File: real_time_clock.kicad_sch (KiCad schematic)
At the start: 4 parts, among them U7 PCF85063A, Y2 Crystal

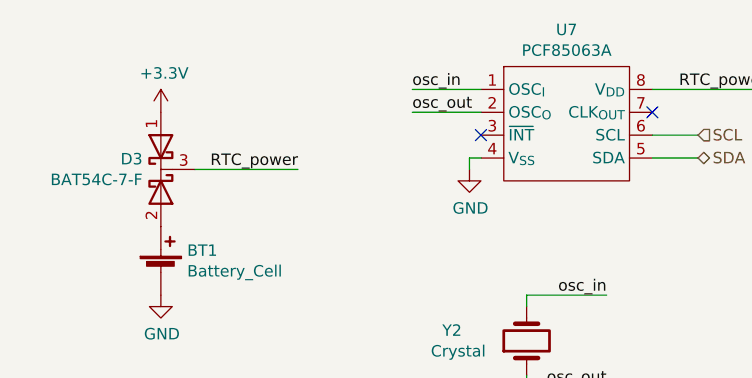
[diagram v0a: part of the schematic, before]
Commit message: more layout: power supply and gpio
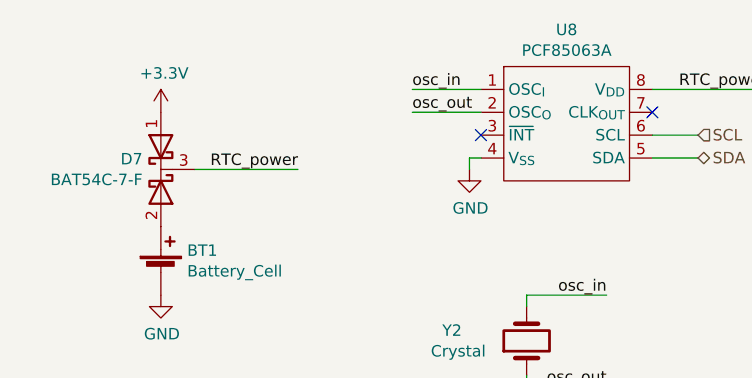
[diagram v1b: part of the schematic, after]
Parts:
- U8: renamed from U7; footprint (none) -> Package_SO:SOIC-8_3.9x4.9mm_P1.27mm
- renumbered D3 to D7
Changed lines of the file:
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@@
   (symbol (lib_id "power:+3.3V") (at 62.23 104.14 0) (unit 1)
     (in_bom yes) (on_board yes)
-    (property "Reference" "#PWR0155" (id 0) (at 62.23 107.95 0)
+    (property "Reference" "#PWR0164" (id 0) (at 62.23 107.95 0)
       (effects (font (size 1.27 1.27)) hide)
     )
@@
   (symbol (lib_id "power:GND") (at 62.23 124.46 0) (unit 1)
     (in_bom yes) (on_board yes)
-    (property "Reference" "#PWR0154" (id 0) (at 62.23 130.81 0)
+    (property "Reference" "#PWR0163" (id 0) (at 62.23 130.81 0)
       (effects (font (size 1.27 1.27)) hide)
     )
@@
   (symbol (lib_id "power:GND") (at 96.52 110.49 0) (unit 1)
     (in_bom yes) (on_board yes)
-    (property "Reference" "#PWR0156" (id 0) (at 96.52 116.84 0)
+    (property "Reference" "#PWR0165" (id 0) (at 96.52 116.84 0)
       (effects (font (size 1.27 1.27)) hide)
     )
@@
   (symbol (lib_id "symbols:BAT54C-7-F") (at 62.23 110.49 0) (unit 1)
     (in_bom yes) (on_board yes)
-    (property "Reference" "D3" (id 0) (at 60.198 109.3406 0)
+    (property "Reference" "D7" (id 0) (at 60.198 109.3406 0)
       (effects (font (size 1.27 1.27)) (justify right))
     )
@@
   (symbol (lib_id "symbols:PCF85063A") (at 107.95 105.41 0) (unit 1)
     (in_bom yes) (on_board yes)
-    (property "Reference" "U7" (id 0) (at 107.315 94.9765 0))
+    (property "Reference" "U8" (id 0) (at 107.315 94.9765 0))
     (property "Value" "PCF85063A" (id 1) (at 107.315 97.2752 0))
-    (property "Footprint" "" (id 2) (at 101.6 102.87 0)
+    (property "Footprint" "Package_SO:SOIC-8_3.9x4.9mm_P1.27mm" (id 2) (at 101.6 102.87 0)
       (effects (font (size 1.27 1.27)) hide)
     )

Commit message: Finished trace routing
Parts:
- removed Y2: Crystal, symbol Device:Crystal
- added JP6, JP7: SolderJumper_3_Open, Jumper:SolderJumper-3_P1.3mm_Open_RoundedPad1.0x1.5mm_NumberLabels, symbol Jumper:SolderJumper_3_Open
- added U10: TCN75, Package_SO:SOIC-8_3.9x4.9mm_P1.27mm, symbol symbols:TCN75
- added Y3: Crystal-CM7V-T1A-32.768kHz, footprints:Crystal-CM7V, symbol symbols:Crystal-CM7V-T1A-32.768kHz
- renumbered D7 to D9, U8 to U9
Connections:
- net GND: now also JP6.3 (B), JP7.3 (B), U10.4 (GND)
- net osc_in: now also Y3.1
- net osc_out: now also Y3.2
- net SCL renamed SCL_{3.3V}
- net SDA renamed SDA_{3.3V}
- new net: JP7.2 (C), U10.5 (A2)
- new net: JP6.2 (C), U10.6 (A1)
- new net +5V: JP6.1 (A), JP7.1 (A), U10.7 (A0), U10.8 (VDD)
- new net SCL_{5V}: U10.2 (SCL)
- new net SDA_{5V}: U10.1 (SDA)
- no-connect marks 2 -> 3
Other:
- note added: "Address Select Jumpers"
- moved on the sheet: BT1, D9, U9

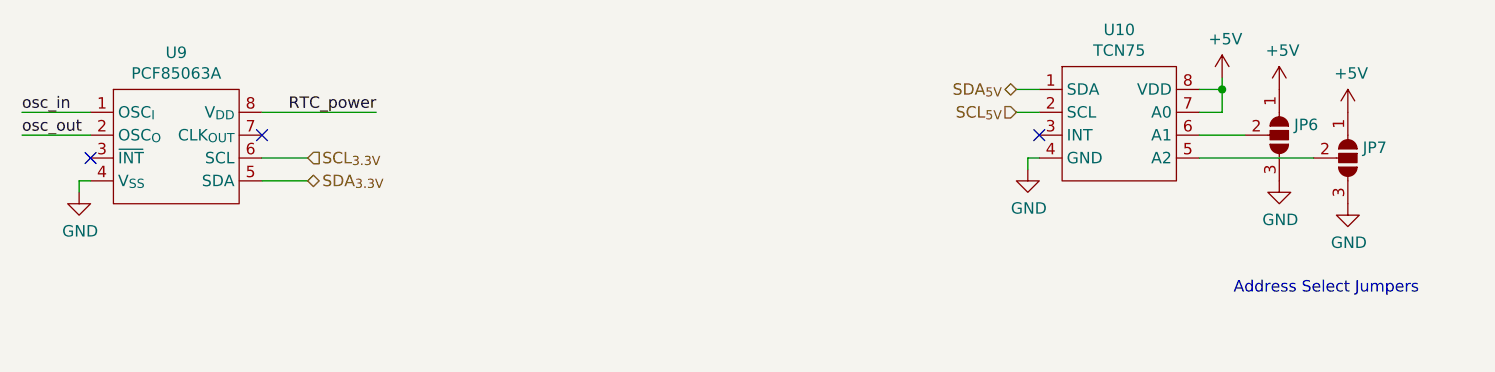
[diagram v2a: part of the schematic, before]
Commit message: Cleaning up
Reassigned reference designators to better match their position on the board.
Moved USB hub IC and related circuits to their own sheet in the schematic.
Tweaked reference designator positions on board to improve visibility.
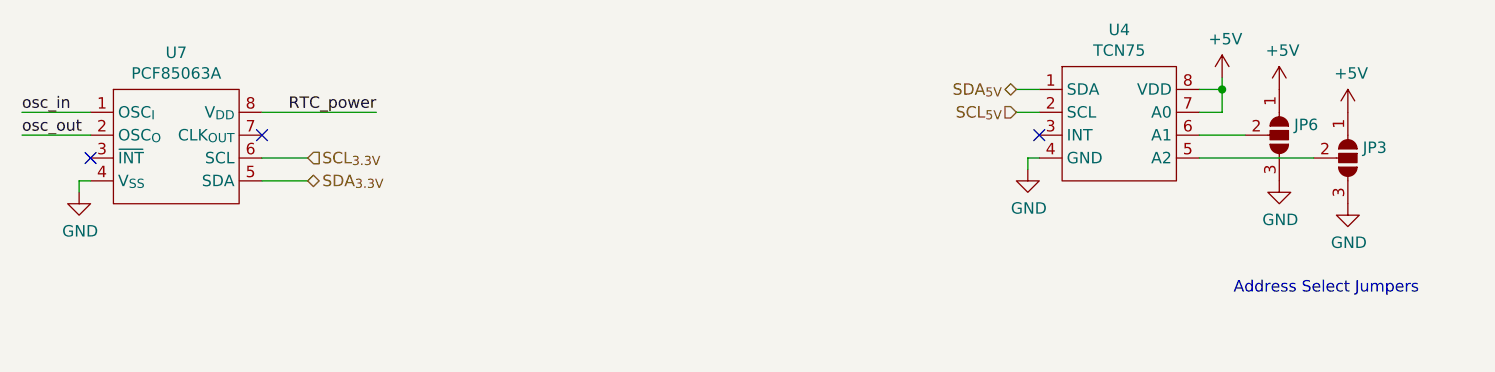
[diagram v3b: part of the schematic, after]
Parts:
- renumbered JP7 to JP3, U10 to U4, U9 to U7
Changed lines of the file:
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@@
   (title_block
     (title "Dennis")
-    (date "2021-02-26")
-    (rev "0.1.2")
+    (date "2021-03-30")
+    (rev "0.1.3")
     (company "eCafe Racer")
   )
   (junction (at 189.23 83.82) (diameter 0.9144) (color 0 0 0 0))
+  (no_connect (at 82.55 88.9))
   (no_connect (at 168.91 88.9))
-  (no_connect (at 82.55 88.9))
   (no_connect (at 63.5 91.44))
   (wire (pts (xy 55.88 86.36) (xy 63.5 86.36))
@@
   (symbol (lib_id "Jumper:SolderJumper_3_Open") (at 203.2 91.44 270) (unit 1)
     (in_bom yes) (on_board yes)
-    (property "Reference" "JP7" (id 0) (at 204.8511 90.2906 90)
+    (property "Reference" "JP3" (id 0) (at 204.8511 90.2906 90)
       (effects (font (size 1.27 1.27)) (justify left))
     )
@@
   (symbol (lib_id "symbols:TCN75") (at 177.8 87.63 0) (unit 1)
     (in_bom yes) (on_board yes)
-    (property "Reference" "U10" (id 0) (at 177.8 77.1965 0))
+    (property "Reference" "U4" (id 0) (at 177.8 77.1965 0))
     (property "Value" "TCN75" (id 1) (at 177.8 79.4952 0))
     (property "Footprint" "Package_SO:SOIC-8_3.9x4.9mm_P1.27mm" (id 2) (at 168.91 83.82 0)
@@
   (symbol (lib_id "symbols:PCF85063A") (at 73.66 90.17 0) (unit 1)
     (in_bom yes) (on_board yes)
-    (property "Reference" "U9" (id 0) (at 73.025 79.7365 0))
+    (property "Reference" "U7" (id 0) (at 73.025 79.7365 0))
     (property "Value" "PCF85063A" (id 1) (at 73.025 82.0352 0))
     (property "Footprint" "Package_SO:SOIC-8_3.9x4.9mm_P1.27mm" (id 2) (at 67.31 87.63 0)

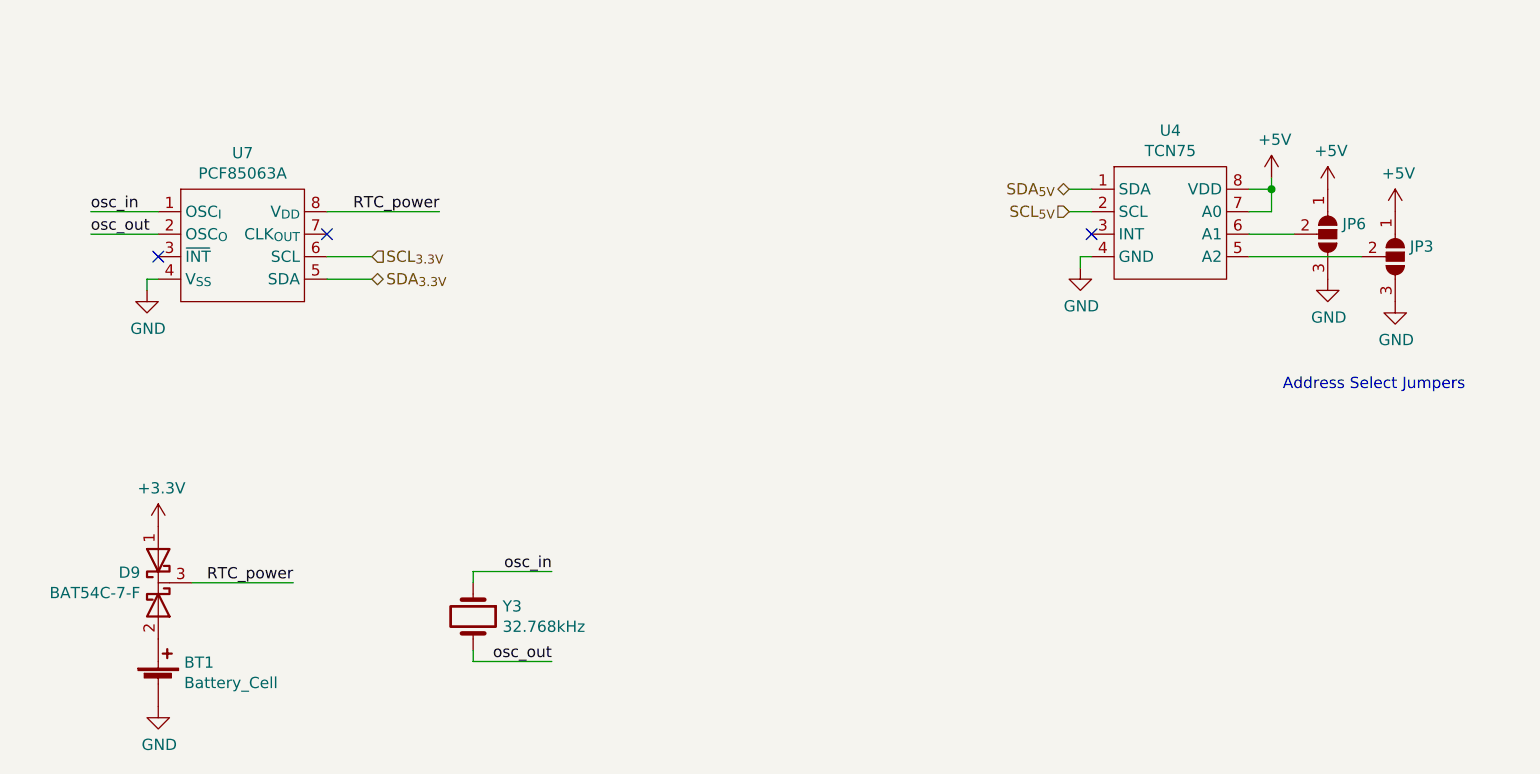
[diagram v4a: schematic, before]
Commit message: components group and placed in roughly the right position
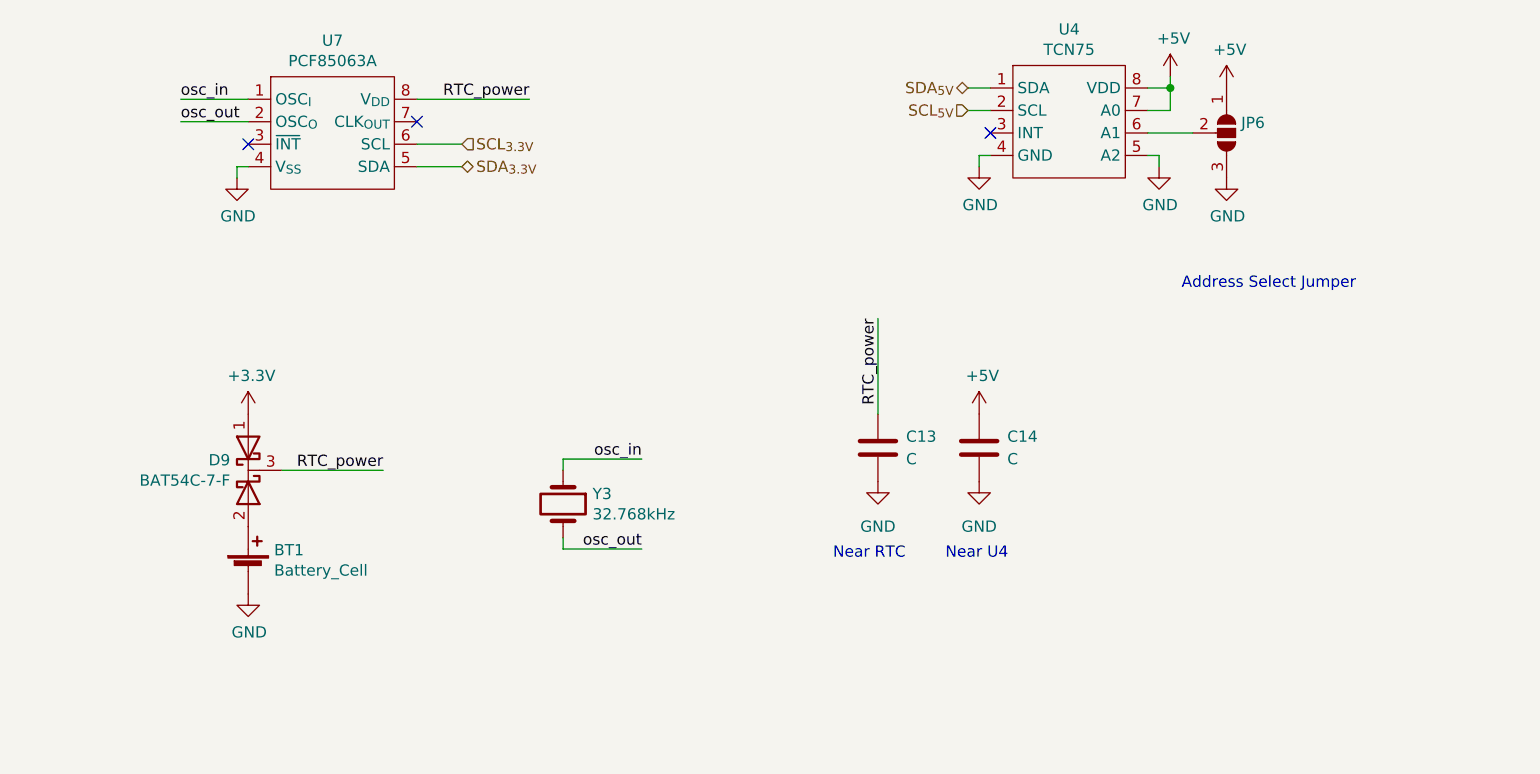
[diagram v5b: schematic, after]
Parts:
- removed JP3: SolderJumper_3_Open, Jumper:SolderJumper-3_P1.3mm_Open_RoundedPad1.0x1.5mm_NumberLabels, symbol Jumper:SolderJumper_3_Open
- added C13, C14: C, Capacitor_SMD:C_0805_2012Metric, symbol Device:C
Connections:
- net +5V: now also C14.1
- net GND: now also U4.5 (A2), C13.2, C14.2
- net RTC_power: now also C13.1
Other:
- note added: "Address Select Jumper"
- note added: "Near RTC"
- note added: "Near U4"
- note removed: "Address Select Jumpers"
- moved on the sheet: BT1, D9, JP6, U4, U7, Y3

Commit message: geographical reannotate
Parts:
- renumbered C13 to C8, D9 to D3, JP6 to JP5, U7 to U2, U4 to U8, Y3 to Y1
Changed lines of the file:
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@@
   (symbol (lib_id "Device:C") (at 144.78 113.03 0) (unit 1)
     (in_bom yes) (on_board yes) (fields_autoplaced)
-    (property "Reference" "C13" (id 0) (at 147.955 111.7599 0)
+    (property "Reference" "C8" (id 0) (at 147.955 111.7599 0)
       (effects (font (size 1.27 1.27)) (justify left))
     )
@@
   (symbol (lib_id "symbols:Crystal-CM7V-T1A-32.768kHz") (at 109.22 119.38 270) (unit 1)
     (in_bom yes) (on_board yes)
-    (property "Reference" "Y3" (id 0) (at 112.548 118.231 90)
+    (property "Reference" "Y1" (id 0) (at 112.548 118.231 90)
       (effects (font (size 1.27 1.27)) (justify left))
     )
@@
   (symbol (lib_id "Jumper:SolderJumper_3_Open") (at 184.15 77.47 270) (unit 1)
     (in_bom yes) (on_board yes)
-    (property "Reference" "JP6" (id 0) (at 185.8011 76.3206 90)
+    (property "Reference" "JP5" (id 0) (at 185.8011 76.3206 90)
       (effects (font (size 1.27 1.27)) (justify left))
     )
@@
   (symbol (lib_id "symbols:BAT54C-7-F") (at 73.66 115.57 0) (unit 1)
     (in_bom yes) (on_board yes)
-    (property "Reference" "D9" (id 0) (at 71.628 114.4206 0)
+    (property "Reference" "D3" (id 0) (at 71.628 114.4206 0)
       (effects (font (size 1.27 1.27)) (justify right))
     )
@@
   (symbol (lib_id "symbols:TCN75") (at 166.37 76.2 0) (unit 1)
     (in_bom yes) (on_board yes)
-    (property "Reference" "U4" (id 0) (at 166.37 65.7665 0))
+    (property "Reference" "U8" (id 0) (at 166.37 65.7665 0))
     (property "Value" "TCN75" (id 1) (at 166.37 68.0652 0))
     (property "Footprint" "Package_SO:SOIC-8_3.9x4.9mm_P1.27mm" (id 2) (at 157.48 72.39 0)
@@
   (symbol (lib_id "symbols:PCF85063A") (at 83.82 77.47 0) (unit 1)
     (in_bom yes) (on_board yes)
-    (property "Reference" "U7" (id 0) (at 83.185 67.0365 0))
+    (property "Reference" "U2" (id 0) (at 83.185 67.0365 0))
     (property "Value" "PCF85063A" (id 1) (at 83.185 69.3352 0))
     (property "Footprint" "Package_SO:SOIC-8_3.9x4.9mm_P1.27mm" (id 2) (at 77.47 74.93 0)

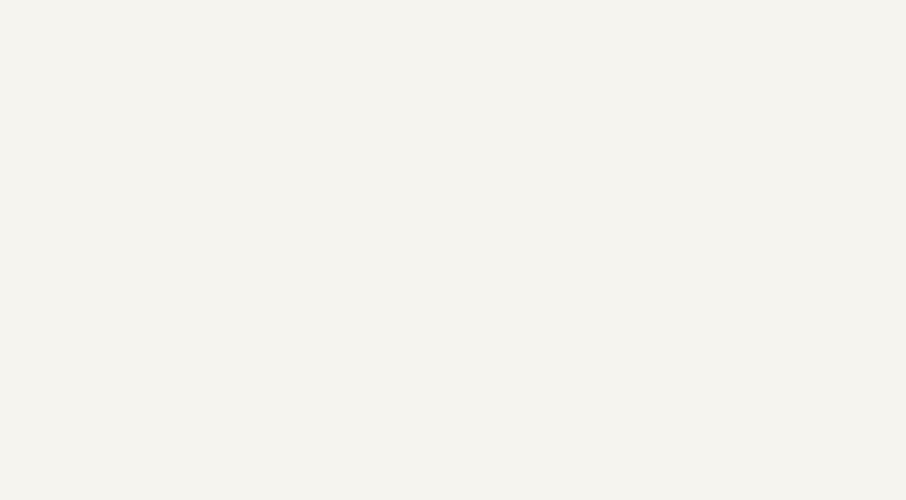
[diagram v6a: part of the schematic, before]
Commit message: cleaned up schematic
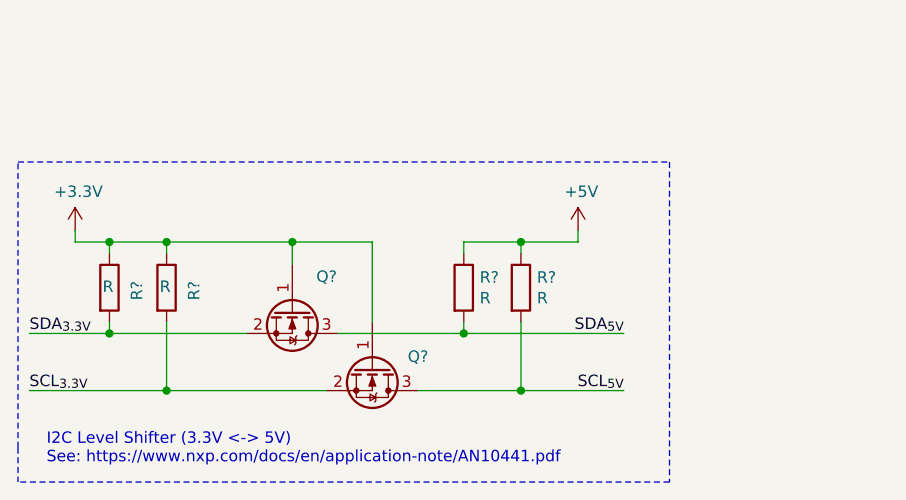
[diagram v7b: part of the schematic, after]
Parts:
- added Q? (x2): DMN62D0U-7, Package_TO_SOT_SMD:SOT-23, symbol symbols:DMN62D0U-7
- added R? (x4): R, Resistor_SMD:R_0805_2012Metric, symbol Device:R
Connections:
- net +3V3: now also Q?.1 (G), Q?.1 (G), R?.1, R?.1
- net +5V: now also R?.1, R?.1
- net SCL_{3.3V}: now also Q?.2 (S), R?.2
- net SCL_{5V}: now also Q?.3 (D), R?.2
- net SDA_{3.3V}: now also Q?.2 (S), R?.2
- net SDA_{5V}: now also Q?.3 (D), R?.2
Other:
- note added: "I2C Level Shifter (3.3V <-> 5V) See: https://www.nxp.com/docs/en/application-note/AN10441.pdf"
